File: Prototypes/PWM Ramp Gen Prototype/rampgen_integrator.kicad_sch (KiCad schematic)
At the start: 15 parts, among them U5 74LV1T04, U6 LT6230

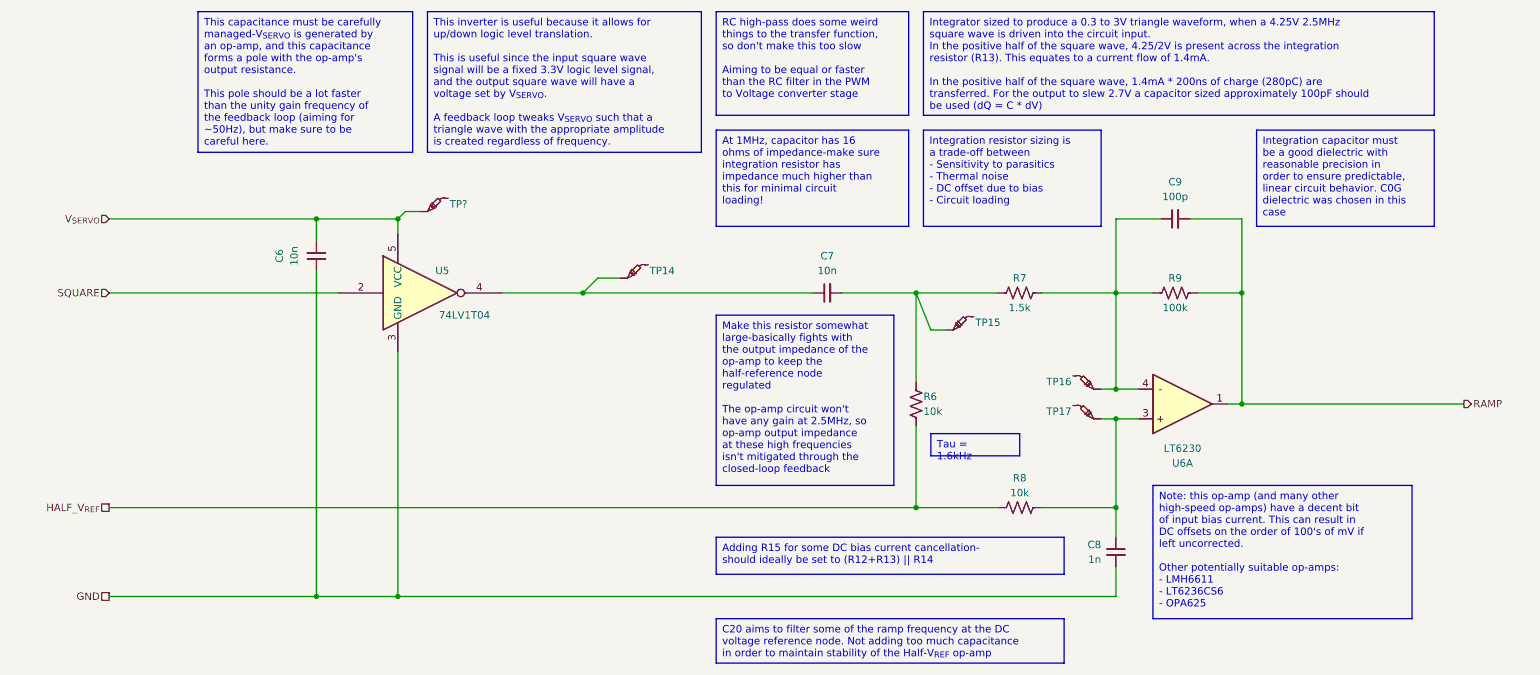
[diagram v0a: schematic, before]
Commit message: Comparator and Op-amp tweaks for BOM consolidation; final layout
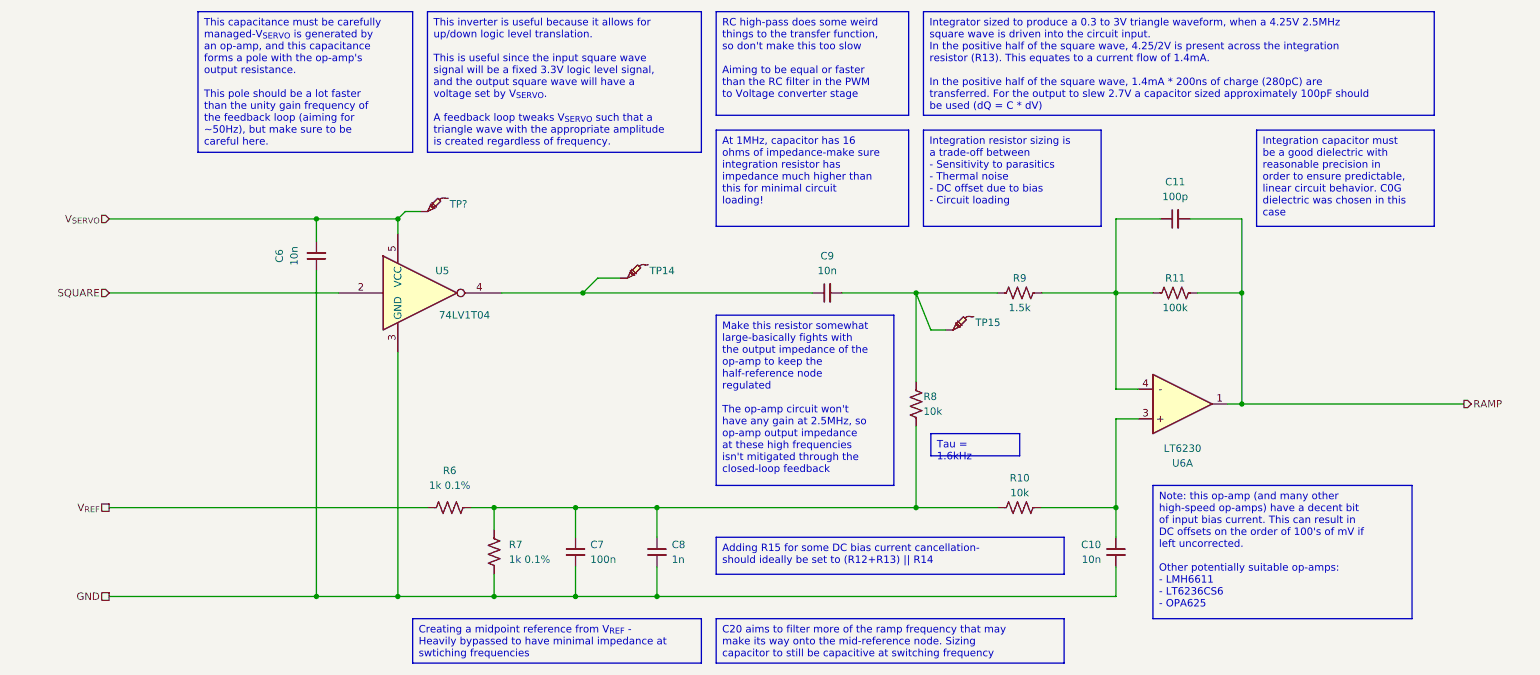
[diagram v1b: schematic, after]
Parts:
- removed TP16, TP17: -, TestPoint:TestPoint_Pad_D2.0mm, symbol Custom-LogicIC:TestPoint
- added C10: 10n, Capacitor_SMD:C_0603_1608Metric_Pad1.08x0.95mm_HandSolder, symbol Custom-Capacitor:CL10B103KB8NNNC
- added C7: 100n, Capacitor_SMD:C_0603_1608Metric_Pad1.08x0.95mm_HandSolder, symbol Custom-Capacitor:CL10B104KB8NNWC
- added R6, R7: 1k 0.1%, Resistor_SMD:R_0603_1608Metric_Pad0.98x0.95mm_HandSolder, symbol Custom-Resistor:RNCF0603BTE1K00
- renumbered C9 to C11, C7 to C9, R8 to R10, R9 to R11, R6 to R8, R7 to R9
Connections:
- net GND: now also C10.2, C7.2, R7.1
- net at R10.2, U6.3: now also C10.1; no longer C8.1
- net HALF_V_{REF}: no longer names the net of R10.1, R8.2
- net HALF_V_{REF}: now also C8.1, C7.1, R6.2, R7.2
- new net V_{REF}: R6.1
